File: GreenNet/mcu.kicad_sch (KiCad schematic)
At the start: 5 parts, among them U1 ESP32-S3-WROOM-1-N16R2

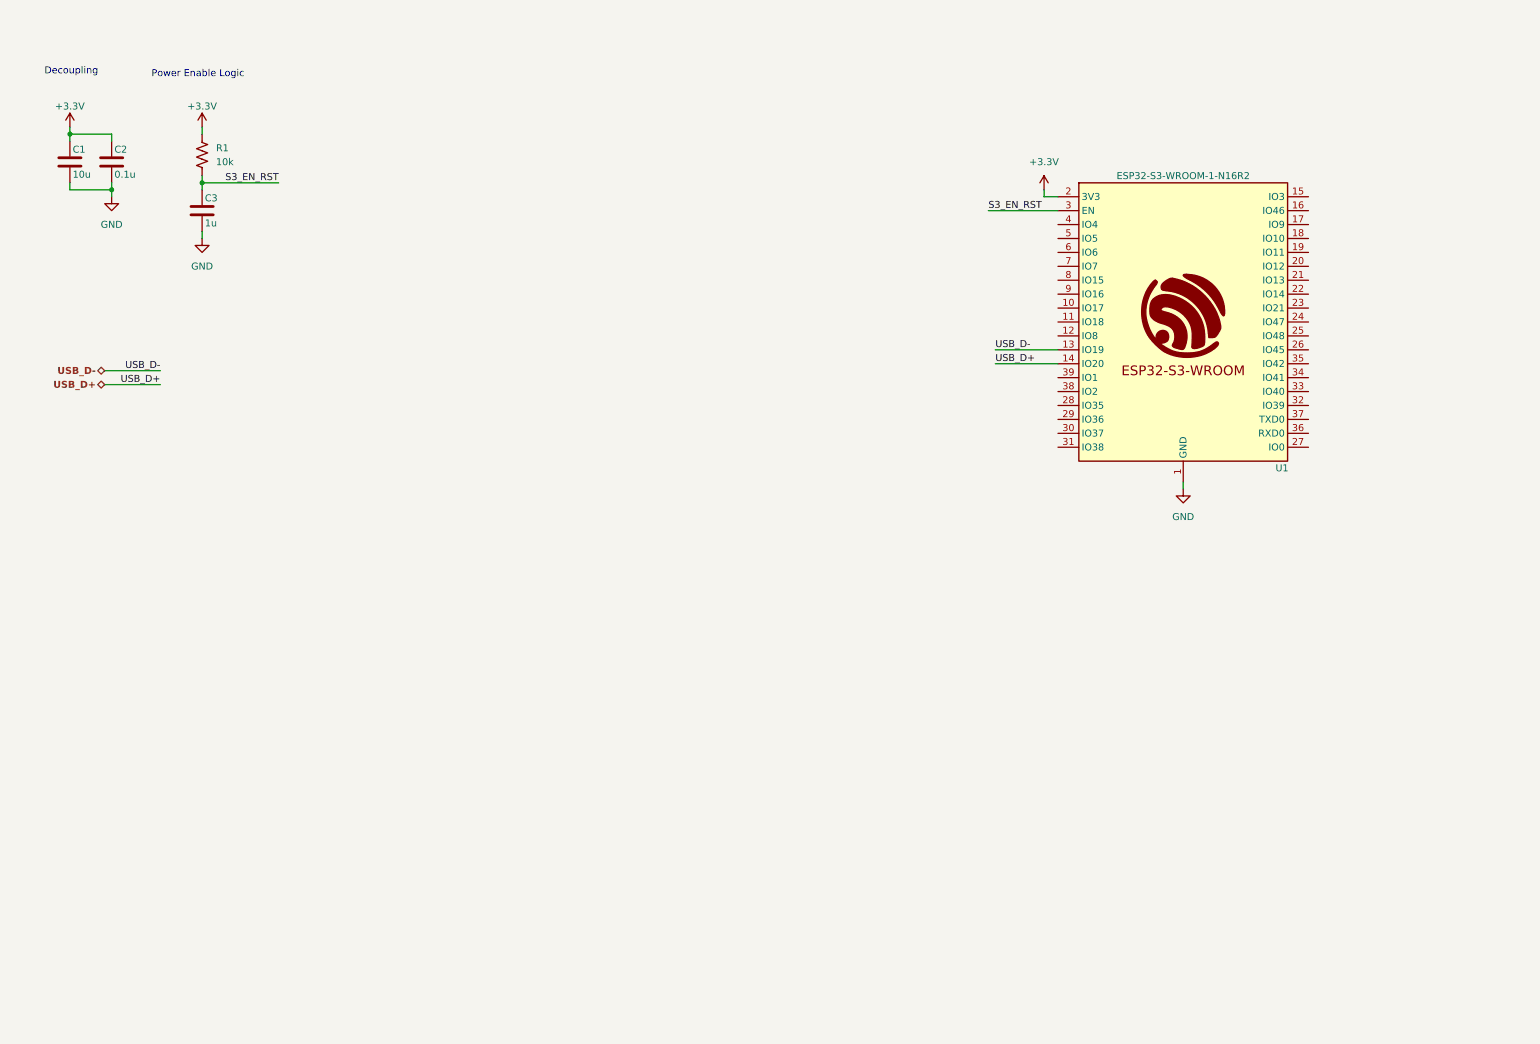
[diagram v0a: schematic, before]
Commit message: finished input schematic
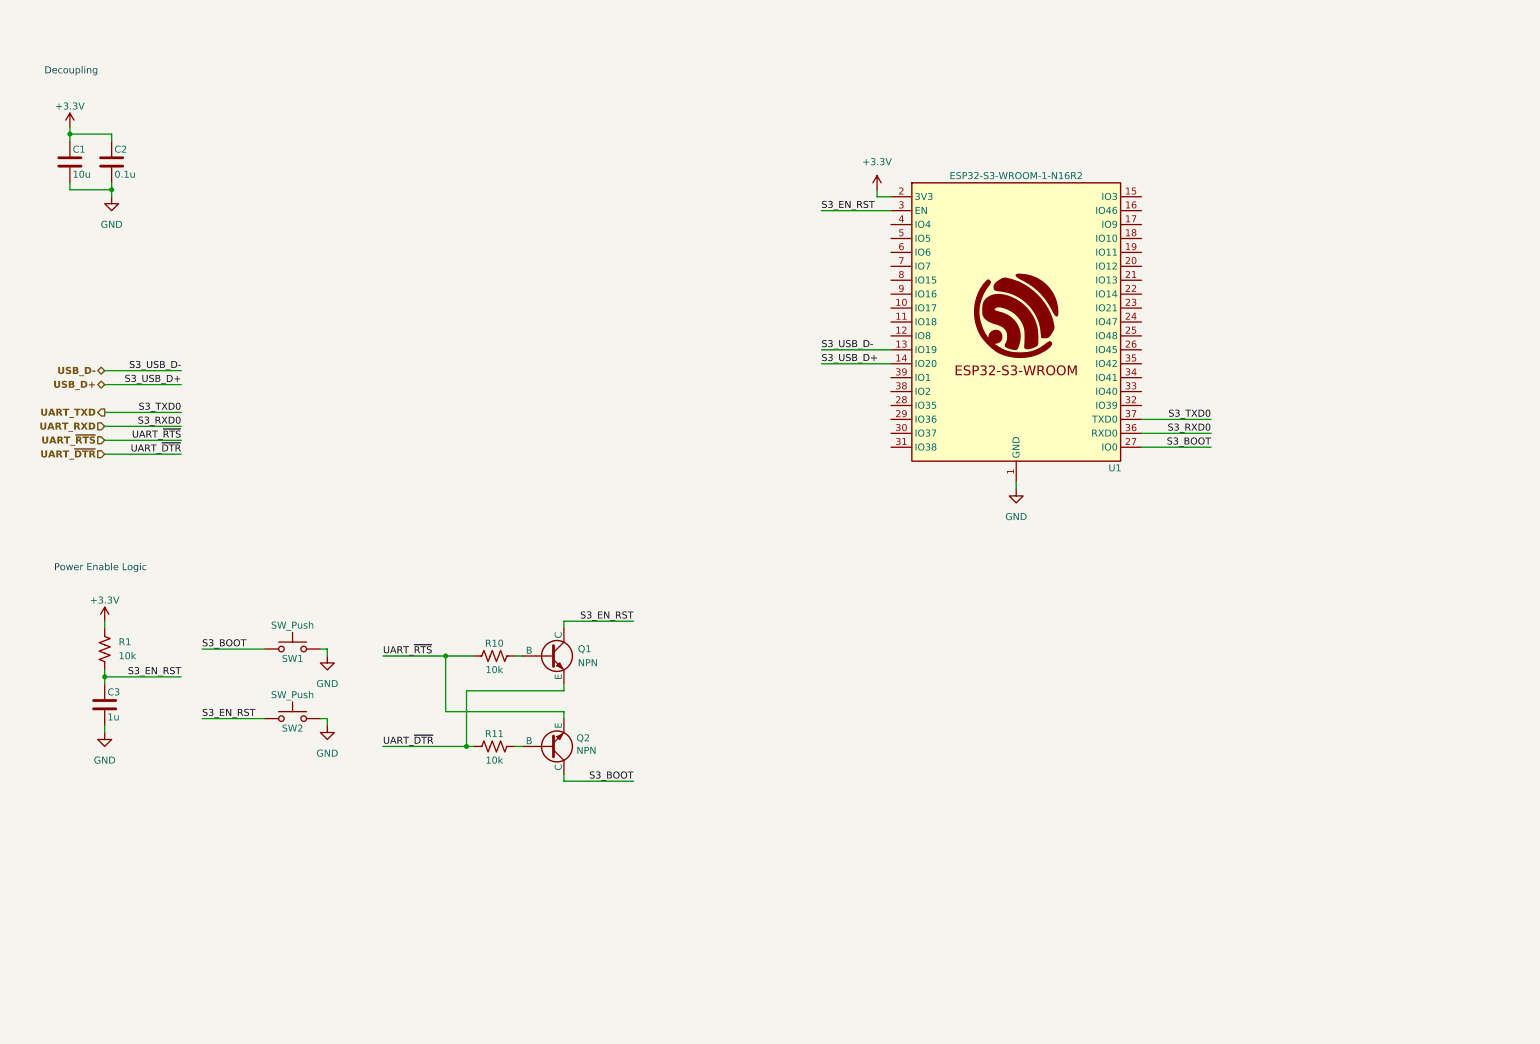
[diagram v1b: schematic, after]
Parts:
- added Q1, Q2: NPN, symbol Simulation_SPICE:NPN
- added R10, R11: 10k, symbol Device:R_US
- added SW1, SW2: SW_Push, symbol Switch:SW_Push
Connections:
- net EPAD: now also SW1.2, SW2.2
- net S3_EN_RST: now also Q1.1 (C), SW2.1
- net S3_BOOT: now reaches U1.27 (IO0)
- net S3_BOOT: now also Q2.1 (C), SW1.1
- net UART_RXD: now reaches U1.36 (RXD0)
- net UART_TXD: now reaches U1.37 (TXD0)
- new net: Q1.2 (B), R10.2
- new net: Q2.2 (B), R11.2
- new net UART_~{DTR}: Q1.3 (E), R11.1
- new net UART_~{RTS}: Q2.3 (E), R10.1
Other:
- moved on the sheet: C3, R1, U1

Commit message: MCU fix
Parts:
- R10, R11: footprint (none) -> Resistor_SMD:R_0805_2012Metric
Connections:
- net EPAD: now also U1.42 (GND), U1.43 (GND), U1.44 (GND), U1.45 (GND), U1.46 (GND), U1.47 (GND), U1.48 (GND), U1.49 (GND)
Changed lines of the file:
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@@
+	)
+	(symbol
+		(lib_id "AA_MCUs:ESP32-S3-WROOM-1-N16R2")
+		(at 191.77 68.58 0)
+		(unit 1)
+		(exclude_from_sim no)
+		(in_bom yes)
+		(on_board yes)
+		(dnp no)
+		(fields_autoplaced yes)
+		(property "Reference" "U1"
+			(at 191.77 38.1 0)
+			(effects
+				(font
+					(size 1.27 1.27)
+				)
+			)
+		)
+		(property "Value" "ESP32-S3-WROOM-1-N16R2"
+			(at 191.77 40.64 0)
+			(effects
+				(font
+					(size 1.27 1.27)
+				)
+			)
+		)
+		(property "Footprint" "AA_MCUs:ESP32S3WROOM1N16R2"
+			(at 217.932 27.686 0)
+			(effects
+				(font
+					(size 1.27 1.27)
+				)
+				(hide yes)
+			)
+		)
+		(property "Datasheet" "https://www.espressif.com/sites/default/files/documentation/esp32-s3-wroom-1_wroom-1u_datasheet_en.pdf"
+			(at 273.812 41.402 0)
+			(effects
+				(font
+					(size 1.27 1.27)
+				)
+				(hide yes)
+			)
+		)
+		(property "Description" "Bluetooth, WiFi 802.11b/g/n, Bluetooth v5.0 Transceiver Module 2.4GHz PCB Trace Surface Mount"
+			(at 217.932 27.686 0)
+			(effects
+				(font
+					(size 1.27 1.27)
+				)
+				(hide yes)
+			)
+		)
+		(pin "42"
+		)
+		(pin "1"
+		)
+		(pin "30"
+		)
+		(pin "17"
+		)
+		(pin "19"
+		)
+		(pin "28"
+		)
+		(pin "23"
+		)
+		(pin "25"
+		)
+		(pin "41"
+		)
+		(pin "34"
+		)
+		(pin "47"
+		)
+		(pin "5"
+		)
+		(pin "26"
+		)
+		(pin "8"
+		)
+		(pin "11"
+		)
+		(pin "2"
+		)
+		(pin "46"
+		)
+		(pin "29"
+		)
+		(pin "12"
+		)
+		(pin "15"
+		)
+		(pin "35"
+		)
+		(pin "4"
+		)
+		(pin "20"
+		)
+		(pin "40"
+		)
+		(pin "44"
+		)
+		(pin "10"
+		)
+		(pin "13"
+		)
+		(pin "31"
+		)
+		(pin "24"
+		)
+		(pin "3"
+		)
+		(pin "37"
+		)
+		(pin "45"
+		)
+		(pin "7"
+		)
+		(pin "27"
+		)
+		(pin "33"
+		)
+		(pin "22"
+		)
+		(pin "39"
+		)
+		(pin "36"
+		)
+		(pin "6"
+		)
+		(pin "21"
+		)
+		(pin "32"
+		)
+		(pin "14"
+		)
+		(pin "16"
+		)
+		(pin "38"
+		)
+		(pin "18"
+		)
+		(pin "43"
+		)
+		(pin "48"
+		)
+		(pin "49"
+		)
+		(pin "9"
+		)
+		(instances
+			(project ""
+				(path "/189669a5-f2fc-4cde-9413-8df80c557655/0ddc2f42-49d8-44b8-acf8-7a4221ab2b02"
+					(reference "U1")
+					(unit 1)
+				)
+			)
+		)
 	)
 	(symbol
@@
 	)
 	(symbol
-		(lib_id "AA_MCUs:ESP32-S3-WROOM-1-N16R2")
-		(at 191.77 68.58 0)
-		(unit 1)
-		(exclude_from_sim no)
-		(in_bom yes)
-		(on_board yes)
-		(dnp no)
-		(property "Reference" "U1"
-			(at 209.804 95.25 0)
-			(effects
-				(font
-					(size 1.27 1.27)
-				)
-			)
-		)
-		(property "Value" "ESP32-S3-WROOM-1-N16R2"
-			(at 191.77 41.91 0)
-			(effects
-				(font
-					(size 1.27 1.27)
-				)
-			)
-		)
-		(property "Footprint" "AA_MCUs:ESP32S3WROOM1N16R2"
-			(at 217.932 27.686 0)
-			(effects
-				(font
-					(size 1.27 1.27)
-				)
-				(hide yes)
-			)
-		)
-		(property "Datasheet" "https://www.espressif.com/sites/default/files/documentation/esp32-s3-wroom-1_wroom-1u_datasheet_en.pdf"
-			(at 273.812 41.402 0)
-			(effects
-				(font
-					(size 1.27 1.27)
-				)
-				(hide yes)
-			)
-		)
-		(property "Description" "Bluetooth, WiFi 802.11b/g/n, Bluetooth v5.0 Transceiver Module 2.4GHz PCB Trace Surface Mount"
-			(at 217.932 27.686 0)
-			(effects
-				(font
-					(size 1.27 1.27)
-				)
-				(hide yes)
-			)
-		)
-		(pin "17"
-		)
-		(pin "14"
-		)
-		(pin "34"
-		)
-		(pin "24"
-		)
-		(pin "15"
-		)
-		(pin "3"
-		)
-		(pin "11"
-		)
-		(pin "40"
-		)
-		(pin "27"
-		)
-		(pin "29"
-		)
-		(pin "18"
-		)
-		(pin "22"
-		)
-		(pin "20"
-		)
-		(pin "31"
-		)
-		(pin "16"
-		)
-		(pin "21"
-		)
-		(pin "37"
-		)
-		(pin "1"
-		)
-		(pin "39"
-		)
-		(pin "10"
-		)
-		(pin "23"
-		)
-		(pin "19"
-		)
-		(pin "30"
-		)
-		(pin "13"
-		)
-		(pin "4"
-		)
-		(pin "5"
-		)
-		(pin "7"
-		)
-		(pin "8"
-		)
-		(pin "32"
-		)
-		(pin "25"
-		)
-		(pin "36"
-		)
-		(pin "41"
-		)
-		(pin "6"
-		)
-		(pin "9"
-		)
-		(pin "2"
-		)
-		(pin "35"
-		)
-		(pin "38"
-		)
-		(pin "26"
-		)
-		(pin "33"
-		)
-		(pin "12"
-		)
-		(pin "28"
-		)
-		(instances
-			(project ""
-				(path "/189669a5-f2fc-4cde-9413-8df80c557655/0ddc2f42-49d8-44b8-acf8-7a4221ab2b02"
-					(reference "U1")
-					(unit 1)
-				)
-			)
-		)
-	)
-	(symbol
 		(lib_id "Device:C")
 		(at 26.67 39.37 0)
@@
 			)
 		)
-		(property "Footprint" ""
+		(property "Footprint" "Resistor_SMD:R_0805_2012Metric"
 			(at 96.774 145.034 90)
 			(effects
@@
 			)
 		)
-		(property "Footprint" ""
+		(property "Footprint" "Resistor_SMD:R_0805_2012Metric"
 			(at 96.774 128.524 90)
 			(effects

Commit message: more sensor work
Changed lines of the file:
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@@
 	(wire
 		(pts
-			(xy 25.4 80.01) (xy 39.37 80.01)
+			(xy 33.02 80.01) (xy 46.99 80.01)
+		)
+		(stroke
+			(width 0)
+			(type default)
+		)
+	)
+	(wire
+		(pts
+			(xy 46.99 97.79) (xy 33.02 97.79)
 		)
 		(stroke
@@
 	(wire
 		(pts
+			(xy 33.02 105.41) (xy 46.99 105.41)
+		)
+		(stroke
+			(width 0)
+			(type default)
+		)
+	)
+	(wire
+		(pts
 			(xy 19.05 44.45) (xy 19.05 43.18)
 		)
@@
 	(wire
 		(pts
-			(xy 39.37 92.71) (xy 25.4 92.71)
+			(xy 46.99 92.71) (xy 33.02 92.71)
 		)
 		(stroke
@@
 	(wire
 		(pts
-			(xy 25.4 77.47) (xy 39.37 77.47)
+			(xy 33.02 77.47) (xy 46.99 77.47)
 		)
 		(stroke
@@
 	(wire
 		(pts
-			(xy 39.37 90.17) (xy 25.4 90.17)
+			(xy 46.99 102.87) (xy 33.02 102.87)
+		)
+		(stroke
+			(width 0)
+			(type default)
+		)
+	)
+	(wire
+		(pts
+			(xy 46.99 90.17) (xy 33.02 90.17)
 		)
 		(stroke
@@
 	(wire
 		(pts
+			(xy 46.99 100.33) (xy 33.02 100.33)
+		)
+		(stroke
+			(width 0)
+			(type default)
+		)
+	)
+	(wire
+		(pts
 			(xy 26.67 34.29) (xy 26.67 35.56)
 		)
@@
 	(wire
 		(pts
-			(xy 39.37 85.09) (xy 25.4 85.09)
-		)
-		(stroke
-			(width 0)
-			(type default)
-		)
-	)
-	(wire
-		(pts
-			(xy 39.37 87.63) (xy 25.4 87.63)
+			(xy 46.99 85.09) (xy 33.02 85.09)
+		)
+		(stroke
+			(width 0)
+			(type default)
+		)
+	)
+	(wire
+		(pts
+			(xy 46.99 87.63) (xy 33.02 87.63)
 		)
 		(stroke
@@
 	)
 	(label "UART_~{RTS}"
-		(at 39.37 90.17 180)
+		(at 46.99 90.17 180)
 		(fields_autoplaced yes)
 		(effects
@@
 	)
 	(label "S3_TXD0"
-		(at 39.37 85.09 180)
+		(at 46.99 85.09 180)
 		(fields_autoplaced yes)
 		(effects
@@
 		)
 	)
+	(label "USB_PD_GPIO"
+		(at 46.99 105.41 180)
+		(fields_autoplaced yes)
+		(effects
+			(font
+				(size 1.27 1.27)
+			)
+			(justify right bottom)
+		)
+	)
 	(label "S3_RXD0"
 		(at 227.33 88.9 180)
@@
 		)
 	)
+	(label "USB_PD_SCL"
+		(at 152.4 53.34 180)
+		(fields_autoplaced yes)
+		(effects
+			(font
+				(size 1.27 1.27)
+			)
+			(justify right bottom)
+		)
+	)
 	(label "UART_~{DTR}"
 		(at 76.2 146.05 0)
@@
 		)
 	)
+	(label "USB_PD_SCL"
+		(at 46.99 100.33 180)
+		(fields_autoplaced yes)
+		(effects
+			(font
+				(size 1.27 1.27)
+			)
+			(justify right bottom)
+		)
+	)
 	(label "S3_EN_RST"
 		(at 156.21 48.26 0)
@@
 	)
 	(label "UART_~{DTR}"
-		(at 39.37 92.71 180)
+		(at 46.99 92.71 180)
+		(fields_autoplaced yes)
+		(effects
+			(font
+				(size 1.27 1.27)
+			)
+			(justify right bottom)
+		)
+	)
+	(label "USB_PD_SDA"
+		(at 152.4 50.8 180)
 		(fields_autoplaced yes)
 		(effects
@@
 	)
 	(label "S3_RXD0"
-		(at 39.37 87.63 180)
+		(at 46.99 87.63 180)
+		(fields_autoplaced yes)
+		(effects
+			(font
+				(size 1.27 1.27)
+			)
+			(justify right bottom)
+		)
+	)
+	(label "USB_PD_INT"
+		(at 152.4 55.88 180)
+		(fields_autoplaced yes)
+		(effects
+			(font
+				(size 1.27 1.27)
+			)
+			(justify right bottom)
+		)
+	)
+	(label "USB_PD_GPIO"
+		(at 152.4 58.42 180)
 		(fields_autoplaced yes)
 		(effects
@@
 		)
 	)
+	(label "USB_PD_SDA"
+		(at 46.99 97.79 180)
+		(fields_autoplaced yes)
+		(effects
+			(font
+				(size 1.27 1.27)
+			)
+			(justify right bottom)
+		)
+	)
 	(label "S3_BOOT"
 		(at 121.92 152.4 180)
@@
 		)
 	)
+	(label "USB_PD_INT"
+		(at 46.99 102.87 180)
+		(fields_autoplaced yes)
+		(effects
+			(font
+				(size 1.27 1.27)
+			)
+			(justify right bottom)
+		)
+	)
 	(label "UART_~{RTS}"
 		(at 76.2 129.54 0)
@@
 	)
 	(label "S3_USB_D+"
-		(at 39.37 80.01 180)
+		(at 46.99 80.01 180)
 		(fields_autoplaced yes)
 		(effects
@@
 	)
 	(label "S3_USB_D-"
-		(at 39.37 77.47 180)
+		(at 46.99 77.47 180)
 		(fields_autoplaced yes)
 		(effects
@@
 	(hierarchical_label "UART_~{DTR}"
 		(shape input)
-		(at 25.4 92.71 180)
+		(at 33.02 92.71 180)
 		(fields_autoplaced yes)
 		(effects
@@
 	(hierarchical_label "UART_~{RTS}"
 		(shape input)
-		(at 25.4 90.17 180)
+		(at 33.02 90.17 180)
 		(fields_autoplaced yes)
 		(effects
@@
 		)
 	)
+	(hierarchical_label "USB_PD_GPIO"
+		(shape bidirectional)
+		(at 33.02 105.41 180)
+		(fields_autoplaced yes)
+		(effects
+			(font
+				(size 1.27 1.27)
+				(bold yes)
+			)
+			(justify right)
+		)
+	)
 	(hierarchical_label "USB_D+"
 		(shape bidirectional)
-		(at 25.4 80.01 180)
+		(at 33.02 80.01 180)
+		(fields_autoplaced yes)
+		(effects
+			(font
+				(size 1.27 1.27)
+				(bold yes)
+			)
+			(justify right)
+		)
+	)
+	(hierarchical_label "USB_PD_INT"
+		(shape input)
+		(at 33.02 102.87 180)
 		(fields_autoplaced yes)
 		(effects
@@
 	(hierarchical_label "UART_RXD"
 		(shape input)
-		(at 25.4 87.63 180)
+		(at 33.02 87.63 180)
 		(fields_autoplaced yes)
 		(effects
@@
 		)
 	)
+	(hierarchical_label "USB_PD_SDA"
+		(shape bidirectional)
+		(at 33.02 97.79 180)
+		(fields_autoplaced yes)
+		(effects
+			(font
+				(size 1.27 1.27)
+				(bold yes)
+			)
+			(justify right)
+		)
+	)
 	(hierarchical_label "UART_TXD"
 		(shape output)
-		(at 25.4 85.09 180)
+		(at 33.02 85.09 180)
 		(fields_autoplaced yes)
 		(effects
@@
 	(hierarchical_label "USB_D-"
 		(shape bidirectional)
-		(at 25.4 77.47 180)
+		(at 33.02 77.47 180)
+		(fields_autoplaced yes)
+		(effects
+			(font
+				(size 1.27 1.27)
+				(bold yes)
+			)
+			(justify right)
+		)
+	)
+	(hierarchical_label "USB_PD_SCL"
+		(shape bidirectional)
+		(at 33.02 100.33 180)
 		(fields_autoplaced yes)
 		(effects
@@
 		(on_board yes)
 		(dnp no)
-		(fields_autoplaced yes)
 		(property "Reference" "Q1"
 			(at 111.76 128.2699 0)
@@
 			)
 		)
-		(property "Description" "Bipolar transistor symbol for simulation only, substrate tied to the emitter"
-			(at 106.68 129.54 0)
-			(effects
-				(font
-					(size 1.27 1.27)
-				)
-				(hide yes)
-			)
-		)
+		(property "Description" "MMDT3904"
+			(at 116.84 132.842 0)
+			(effects
+				(font
+					(size 1.27 1.27)
+				)
+			)
+		)

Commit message: significant progress
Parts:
- removed Q1, Q2: NPN, symbol Simulation_SPICE:NPN
- removed SW1, SW2: SW_Push, symbol Switch:SW_Push
- added D14, D15: D5V0M1U2S9, AA_Diodes:D5V0M1U2S9Q, symbol Device:D_Zener_Filled
- added H1, H2, H3, H4: MountingHole_Pad, MountingHole:MountingHole_2.5mm_Pad, symbol Mechanical:MountingHole_Pad
- added J2, J3, J5: 3_Pin_Conn, AA_Connectors:61300311121, symbol Connector:Conn_01x03_Pin
- added J6: Conn_01x14_Pin, AA_Connectors:CONN_PH1-14-UA_ADM, symbol Connector:Conn_01x14_Pin
- added Q8: MMDT3904, Package_TO_SOT_SMD:SOT-363_SC-70-6, symbol Transistor_BJT:MMDT3904
- added R28, R29, R30, R31, R32, R33, R34: 10k, Resistor_SMD:R_0805_2012Metric, symbol Device:R_US
- added SW1, SW3: SW_MEC_5E, AA_Switches:18259106, symbol Switch:SW_MEC_5E
- added TP3, TP31, TP32, TP5, TP7, TP8: TestPoint, AA_TestPoints:RCWCTE, symbol Connector:TestPoint
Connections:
- net +3.3V: now also J2.1 (Pin_1), J3.1 (Pin_1), J5.1 (Pin_1), R28.2, R29.2, R30.2, R31.2, R32.2, R33.2, R34.2
- net EPAD: now also D14.2 (A), D15.2 (A), H1.1, H2.1, H3.1, H4.1, J2.3 (Pin_3), J3.3 (Pin_3), J5.3 (Pin_3), SW1.3 (K), SW1.4 (A), SW3.3 (K), SW3.4 (A)
- net S3_BOOT: now also D14.1 (K), Q8.6 (C1), SW3.1, SW3.2, TP32.1
- net S3_EN_RST: now also D15.1 (K), Q8.3 (C2), SW1.1, SW1.2, TP31.1
- net UART_~{DTR}: now also Q8.4 (E2)
- net UART_~{RTS}: now also Q8.1 (E1)
- net USB_PD_GPIO: now also U1.25 (IO48)
- net USB_PD_INT: now also U1.24 (IO47), R33.1
- net S3_IO17: now reaches U1.10 (IO17)
- net S3_IO17: now also J6.8 (Pin_8)
- net S3_IO18: now reaches U1.11 (IO18)
- net S3_IO18: now also J6.9 (Pin_9)
- net LCD_EN: now reaches U1.12 (IO8)
- net S3_IO3: now reaches U1.15 (IO3)
- net S3_IO3: now also J2.2 (Pin_2)
- net S3_IO46: now reaches U1.16 (IO46)
- net S3_IO46: now also J5.2 (Pin_2)
- net S3_IO9: now reaches U1.17 (IO9)
- net S3_IO9: now also J6.3 (Pin_3)
- net S3_IO10: now reaches U1.18 (IO10)
- net S3_IO10: now also J6.4 (Pin_4)
- net S3_IO11: now reaches U1.19 (IO11)
- net S3_IO11: now also J6.5 (Pin_5)
- net PWR_SDA: now reaches U1.20 (IO12)
- net PWR_SDA: now also R28.1, TP7.1
- net PWR_SCL: now reaches U1.21 (IO13)
- net PWR_SCL: now also R29.1, TP8.1
- net S3_IO14: now reaches U1.22 (IO14)
- net S3_IO14: now also J6.6 (Pin_6)
- net S3_IO21: now reaches U1.23 (IO21)
- net S3_IO21: now also J6.10 (Pin_10)
- net S3_IO45: now reaches U1.26 (IO45)
- net S3_IO45: now also J3.2 (Pin_2)
- net S3_IO35: now reaches U1.28 (IO35)
- net S3_IO35: now also J6.11 (Pin_11)
- net S3_IO36: now reaches U1.29 (IO36)
- net S3_IO36: now also J6.12 (Pin_12)
- net S3_IO37: now reaches U1.30 (IO37)
- net S3_IO37: now also J6.13 (Pin_13)
- net S3_IO38: now reaches U1.31 (IO38)
- net S3_IO38: now also J6.14 (Pin_14)
- net BAT_EN2: now reaches U1.32 (IO39)
- net BAT_EN1: now reaches U1.33 (IO40)
- net BAT_~{CE}: now reaches U1.34 (IO41)
- net BAT_INT: now reaches U1.35 (IO42)
- net BAT_INT: now also R30.1
- net S3_IO2: now reaches U1.38 (IO2)
- net S3_IO2: now also J6.2 (Pin_2)
- net S3_IO1: now reaches U1.39 (IO1)
- net S3_IO1: now also J6.1 (Pin_1)
- net PERI_SDA: now reaches U1.4 (IO4)
- net PERI_SDA: now also R31.1, TP3.1
- net PERI_SCL: now reaches U1.5 (IO5)
- net PERI_SCL: now also R32.1, TP5.1
- net SOIL_EN: now reaches U1.6 (IO6)
- net SOIL_SENSE: now reaches U1.7 (IO7)
- net LTR_INT: now reaches U1.8 (IO15)
- net LTR_INT: now also R34.1
- net S3_IO16: now reaches U1.9 (IO16)
- net S3_IO16: now also J6.7 (Pin_7)
- net at R10.2: now also Q8.5 (B2)
- net at R11.2: now also Q8.2 (B1)
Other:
- note added: "Auto Reset"
- note added: "Extra GPIO Output"
- note added: "INPUT PINS"
- note added: "I^{2}C Pull-ups"
- note added: "MICROCONTROLLER"
- note added: "Reset Switches"
- note added: "Strapping Pin Settings"
- note added: "TEST POINTS"
- moved on the sheet: C1, C2, C3, R1, R10, R11, U1

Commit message: update
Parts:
- removed Q8: MMDT3904, Package_TO_SOT_SMD:SOT-363_SC-70-6, symbol Transistor_BJT:MMDT3904
- removed R10, R11: 10k, Resistor_SMD:R_0805_2012Metric, symbol Device:R_US
- removed TP7, TP8: TestPoint, AA_TestPoints:RCWCTE, symbol Connector:TestPoint
- added Q1: MMDT3904, Package_TO_SOT_SMD:SOT-363_SC-70-6, symbol Transistor_BJT:MMDT3904
- added R2, R3: 10k, Resistor_SMD:R_0805_2012Metric, symbol Device:R_US
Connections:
- net S3_BOOT: now also Q1.6 (C1)
- net S3_EN_RST: now also Q1.3 (C2)
- net UART_~{DTR}: now also Q1.4 (E2), R3.1
- net UART_~{RTS}: now also Q1.1 (E1), R2.1
- net USB_PD_GPIO renamed USB_GPIO
- net USB_PD_INT renamed USB_HPI_INT
- new net: Q1.5 (B2), R2.2
- new net: Q1.2 (B1), R3.2
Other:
- moved on the sheet: TP31, TP32

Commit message: schematic FINAL
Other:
- note added: "MOUNTING HOLES"
- moved on the sheet: H1, H2, H3, H4, TP3, TP31, TP32, TP5
